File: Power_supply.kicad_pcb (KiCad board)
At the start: 2 copper layers, 116 x 65 mm, 46 parts, among them J1 Transformers, J2 240V, J20 HV_Transformer, J21 LV_Transformer, J22 220V, J23 Transformers, J25 Anodes_enable, J3 6V3, J6 Conn_01x07, Q1 STP4NK60ZFP(MJE13003)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

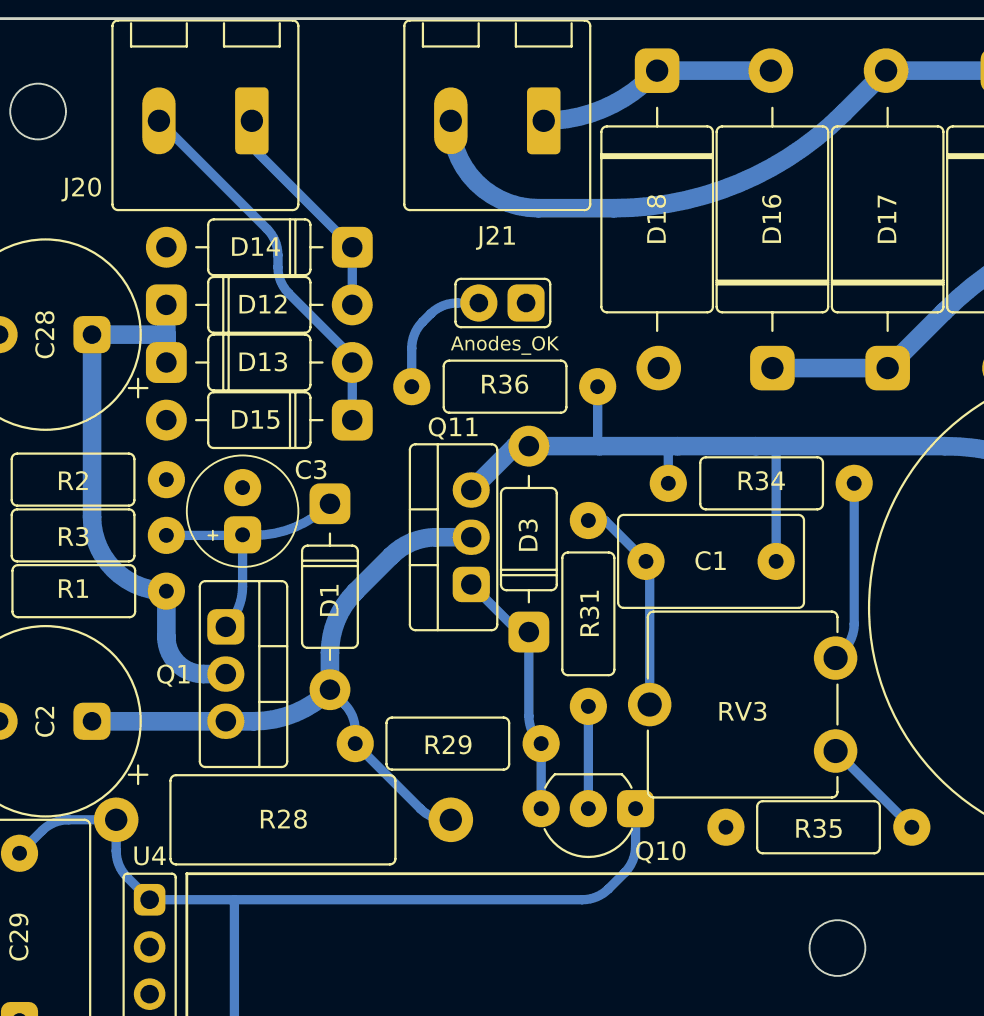
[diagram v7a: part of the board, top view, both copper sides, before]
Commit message: More rounded corners!
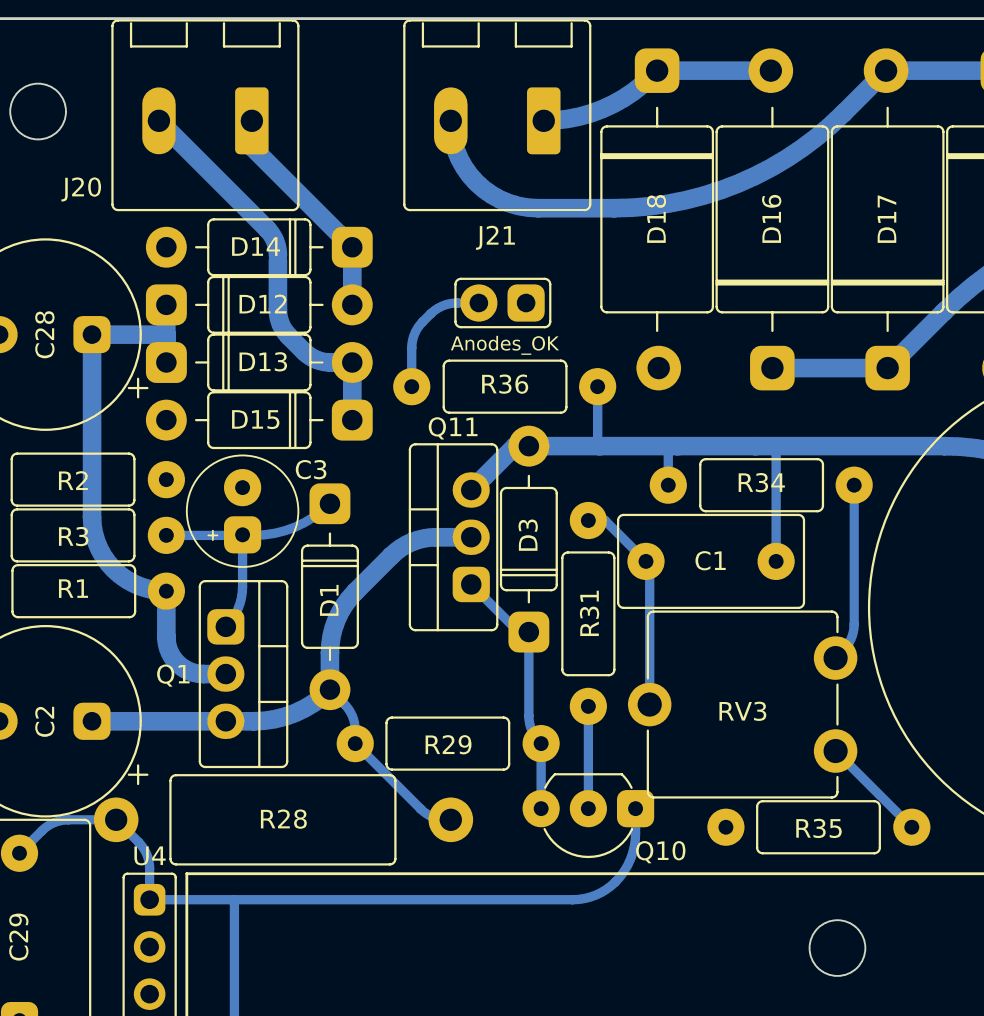
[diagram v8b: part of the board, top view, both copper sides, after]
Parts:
- moved R34 0.10 mm to (135.9, 110.1)
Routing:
- net Net-(D13-A): track 20.2 -> 21.3 mm
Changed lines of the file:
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@@
   )
   (footprint "spdf1626_lib:R_THT_025W" (layer "F.Cu")
-    (at 135.9 110)
+    (at 135.9 110.1)
     (descr "Resistor, Axial_DIN0207 series, Axial, Horizontal, pin pitch=10.16mm, 0.25W = 1/4W, length*diameter=6.3*2.5mm^2, http://cdn-reichelt.de/documents/datenblatt/B400/1_4W%23YAG.pdf")
     (tags "Resistor Axial_DIN0207 series Axial Horizontal pin pitch 10.16mm 0.25W = 1/4W length 6.3mm diameter 2.5mm")
@@
   (arc (start 161.335995 97.475995) (mid 164.685536 99.714087) (end 168.63659 100.5) (width 1) (layer "B.Cu") (net 3))
   (arc (start 159.1 95.24) (mid 151.856785 96.680766) (end 145.716279 100.783721) (width 1) (layer "B.Cu") (net 3))
+  (segment (start 130.9 110.1) (end 130.9 108) (width 0.5) (layer "B.Cu") (net 4))
   (segment (start 122.66 108) (end 120.3 110.36) (width 1) (layer "B.Cu") (net 4))
   (segment (start 135.6 108) (end 131.4 108) (width 1) (layer "B.Cu") (net 4))
@@
   (segment (start 136.7 114.2) (end 136.7 108) (width 0.5) (layer "B.Cu") (net 4))
   (segment (start 127.1 107.9) (end 127.2 108) (width 0.5) (layer "B.Cu") (net 4))
-  (segment (start 130.9 110) (end 130.9 108) (width 0.5) (layer "B.Cu") (net 4))
   (arc (start 154.7 111.7) (mid 150.601691 108.961604) (end 145.767384 108) (width 1) (layer "B.Cu") (net 4))
   (segment (start 108.59584 122.8) (end 107.1 122.8) (width 1) (layer "B.Cu") (net 5))
@@
   (segment (start 74 115.5) (end 74 118.3) (width 1) (layer "B.Cu") (net 10))
   (arc (start 74 118.3) (mid 74.585786 119.714214) (end 76 120.3) (width 1) (layer "B.Cu") (net 10))
-  (segment (start 127.685787 131.814213) (end 128.554214 130.945786) (width 0.5) (layer "B.Cu") (net 11))
   (segment (start 104.878257 142.56) (end 103 142.56) (width 0.5) (layer "B.Cu") (net 11))
   (segment (start 97.214213 128.685787) (end 96 129.9) (width 0.5) (layer "B.Cu") (net 11))
-  (segment (start 101.2 128.1) (end 101.2 129.771573) (width 0.5) (layer "B.Cu") (net 11))
+  (segment (start 102.414213 129.314213) (end 101.2 128.1) (width 0.5) (layer "B.Cu") (net 11))
   (segment (start 101.2 128.1) (end 98.628427 128.1) (width 0.5) (layer "B.Cu") (net 11))
   (segment (start 107.56 132.4) (end 107.56 139.878257) (width 0.5) (layer "B.Cu") (net 11))
-  (segment (start 107.56 132.4) (end 126.271573 132.4) (width 0.5) (layer "B.Cu") (net 11))
+  (segment (start 107.56 132.4) (end 125.746884 132.4) (width 0.5) (layer "B.Cu") (net 11))
   (segment (start 107.56 132.4) (end 103 132.4) (width 0.5) (layer "B.Cu") (net 11))
-  (segment (start 101.785787 131.185787) (end 103 132.4) (width 0.5) (layer "B.Cu") (net 11))
-  (segment (start 129.14 129.531573) (end 129.14 127.5) (width 0.5) (layer "B.Cu") (net 11))
-  (arc (start 101.2 129.771573) (mid 101.352241 130.53694) (end 101.785787 131.185787) (width 0.5) (layer "B.Cu") (net 11))
-  (arc (start 127.685787 131.814213) (mid 127.03694 132.247759) (end 126.271573 132.4) (width 0.5) (layer "B.Cu") (net 11))
+  (segment (start 103 132.4) (end 103 130.728427) (width 0.5) (layer "B.Cu") (net 11))
+  (segment (start 129.14 128.828133) (end 129.14 127.5) (width 0.5) (layer "B.Cu") (net 11))
+  (arc (start 103 130.728427) (mid 102.847759 129.96306) (end 102.414213 129.314213) (width 0.5) (layer "B.Cu") (net 11))
+  (arc (start 128.056797 131.443203) (mid 126.997 132.151337) (end 125.746884 132.4) (width 0.5) (layer "B.Cu") (net 11))
   (arc (start 107.56 139.878257) (mid 106.774536 141.774536) (end 104.878257 142.56) (width 0.5) (layer "B.Cu") (net 11))
-  (arc (start 128.554214 130.945786) (mid 128.987759 130.29694) (end 129.14 129.531573) (width 0.5) (layer "B.Cu") (net 11))
+  (arc (start 128.056797 131.443203) (mid 128.858487 130.243393) (end 129.14 128.828133) (width 0.5) (layer "B.Cu") (net 11))
   (arc (start 97.214213 128.685787) (mid 97.86306 128.252241) (end 98.628427 128.1) (width 0.5) (layer "B.Cu") (net 11))
   (segment (start 123.985787 123.925787) (end 124.06 124) (width 0.5) (layer "B.Cu") (net 12))
@@
   (segment (start 124.06 124) (end 124.06 127.5) (width 0.5) (layer "B.Cu") (net 12))
   (arc (start 123.4 122.511573) (mid 123.552241 123.27694) (end 123.985787 123.925787) (width 0.5) (layer "B.Cu") (net 12))
-  (segment (start 113.9 97.3) (end 108.5 91.9) (width 0.5) (layer "B.Cu") (net 13))
-  (segment (start 108.5 91.9) (end 108.5 90.5) (width 0.5) (layer "B.Cu") (net 13))
-  (segment (start 113.9 100.4) (end 113.9 97.3) (width 0.5) (layer "B.Cu") (net 13))
-  (segment (start 109.314213 96.314213) (end 103.5 90.5) (width 0.5) (layer "B.Cu") (net 14))
-  (segment (start 113.9 103.2) (end 110.485786 99.785786) (width 0.5) (layer "B.Cu") (net 14))
-  (segment (start 113.9 106.6) (end 113.9 103.2) (width 0.5) (layer "B.Cu") (net 14))
-  (segment (start 109.9 98.371573) (end 109.9 97.728427) (width 0.5) (layer "B.Cu") (net 14))
-  (arc (start 109.314213 96.314213) (mid 109.747759 96.96306) (end 109.9 97.728427) (width 0.5) (layer "B.Cu") (net 14))
-  (arc (start 110.485786 99.785786) (mid 110.052241 99.13694) (end 109.9 98.371573) (width 0.5) (layer "B.Cu") (net 14))
+  (segment (start 113.9 97.3) (end 108.5 91.9) (width 1) (layer "B.Cu") (net 13))
+  (segment (start 108.5 91.9) (end 108.5 90.5) (width 1) (layer "B.Cu") (net 13))
+  (segment (start 113.9 100.4) (end 113.9 97.3) (width 1) (layer "B.Cu") (net 13))
+  (segment (start 109.314213 96.314213) (end 103.5 90.5) (width 1) (layer "B.Cu") (net 14))
+  (segment (start 113.9 106.6) (end 113.9 103.5) (width 1) (layer "B.Cu") (net 14))
+  (segment (start 111.314213 102.914213) (end 110.485786 102.085786) (width 1) (layer "B.Cu") (net 14))
+  (segment (start 113.9 103.5) (end 112.728427 103.5) (width 1) (layer "B.Cu") (net 14))
+  (segment (start 109.9 98) (end 109.9 97.728427) (width 0.5) (layer "B.Cu") (net 14))
+  (segment (start 109.9 100.671573) (end 109.9 98) (width 1) (layer "B.Cu") (net 14))
+  (arc (start 110.485786 102.085786) (mid 110.052241 101.43694) (end 109.9 100.671573) (width 1) (layer "B.Cu") (net 14))
+  (arc (start 111.314213 102.914213) (mid 111.96306 103.347759) (end 112.728427 103.5) (width 1) (layer "B.Cu") (net 14))
+  (arc (start 109.314213 96.314213) (mid 109.747759 96.96306) (end 109.9 97.728427) (width 1) (layer "B.Cu") (net 14))
   (segment (start 130.004148 88.095852) (end 130.3 87.8) (width 1) (layer "B.Cu") (net 15))
   (segment (start 136.415 87.8) (end 130.3 87.8) (width 1) (layer "B.Cu") (net 15))
@@
   (arc (start 78.414213 142.385787) (mid 78.847759 141.73694) (end 79 140.971573) (width 1) (layer "B.Cu") (net 21))
   (segment (start 139.9 119.4) (end 140.314214 118.985786) (width 0.5) (layer "B.Cu") (net 22))
-  (segment (start 140.9 117.571573) (end 140.9 110) (width 0.5) (layer "B.Cu") (net 22))
-  (arc (start 140.314214 118.985786) (mid 140.747759 118.33694) (end 140.9 117.571573) (width 0.5) (layer "B.Cu") (net 22))
+  (segment (start 140.9 117.571573) (end 140.9 110.1) (width 0.5) (layer "B.Cu") (net 22))
+  (arc (start 140.314214 118.985786) (mid 140.74775 118.336938) (end 140.9 117.571573) (width 0.5) (layer "B.Cu") (net 22))
   (segment (start 139.9 124.4) (end 144 128.5) (width 0.5) (layer "B.Cu") (net 23))
   (segment (start 126.6 127.5) (end 126.6 122) (width 0.5) (layer "B.Cu") (net 24))
